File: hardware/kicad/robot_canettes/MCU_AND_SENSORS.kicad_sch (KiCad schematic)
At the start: 0 parts

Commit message: Ajout du STM32 et de son alimentation de base
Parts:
- added U1: STM32G431RBTx, Package_QFP:LQFP-64_10x10mm_P0.5mm, symbol MCU_ST_STM32G4:STM32G431RBTx
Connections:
- new net +3V3: U1.1 (VBAT), U1.16 (VDD), U1.28 (VREF+), U1.29 (VDDA), U1.32 (VDD), U1.48 (VDD), U1.64 (VDD)
- new net GND: U1.15 (VSS), U1.27 (VSSA), U1.31 (VSS), U1.47 (VSS), U1.63 (VSS)
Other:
- company: (none) -> ENSEA
- title: (none) -> MCU_AND_SENSORS

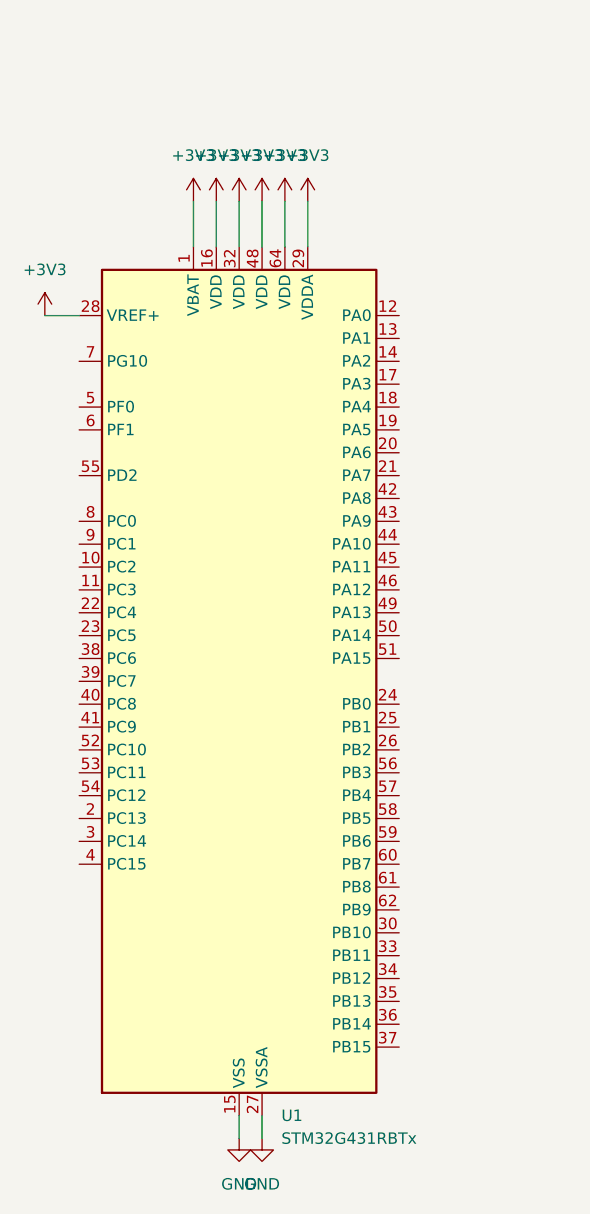
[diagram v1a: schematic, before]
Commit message: Ajout découplage VDD/VDDA/VBAT + condensateur NRST
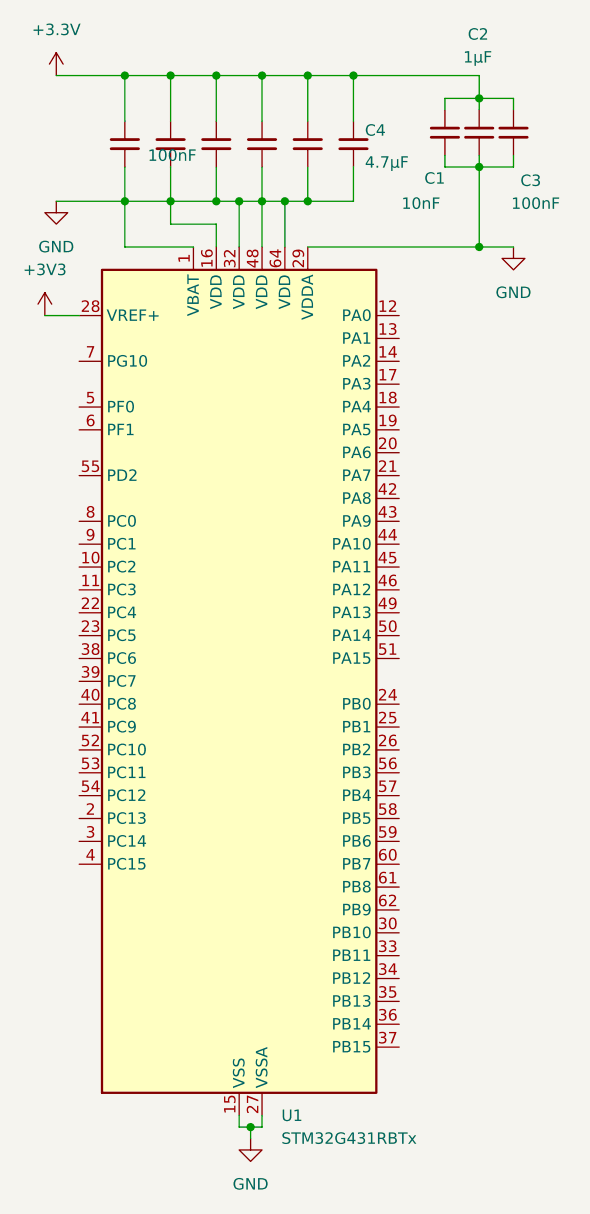
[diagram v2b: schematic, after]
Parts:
- added C1: 10nF, symbol Device:C_Small
- added C2: 1µF, symbol Device:C_Small
- added C3, C5, C6, C7, C8, C9: 100nF, symbol Device:C_Small
- added C4: 4.7µF, symbol Device:C_Small
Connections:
- net +3V3: no longer U1.1 (VBAT), U1.16 (VDD), U1.29 (VDDA), U1.32 (VDD), U1.48 (VDD), U1.64 (VDD)
- net GND: now also U1.1 (VBAT), U1.16 (VDD), U1.29 (VDDA), U1.32 (VDD), U1.48 (VDD), U1.64 (VDD), C1.2, C2.2, C3.2, C4.2, C5.2, C6.2, C7.2, C8.2, C9.2
- new net +3.3V: C1.1, C2.1, C3.1, C4.1, C5.1, C6.1, C7.1, C8.1, C9.1

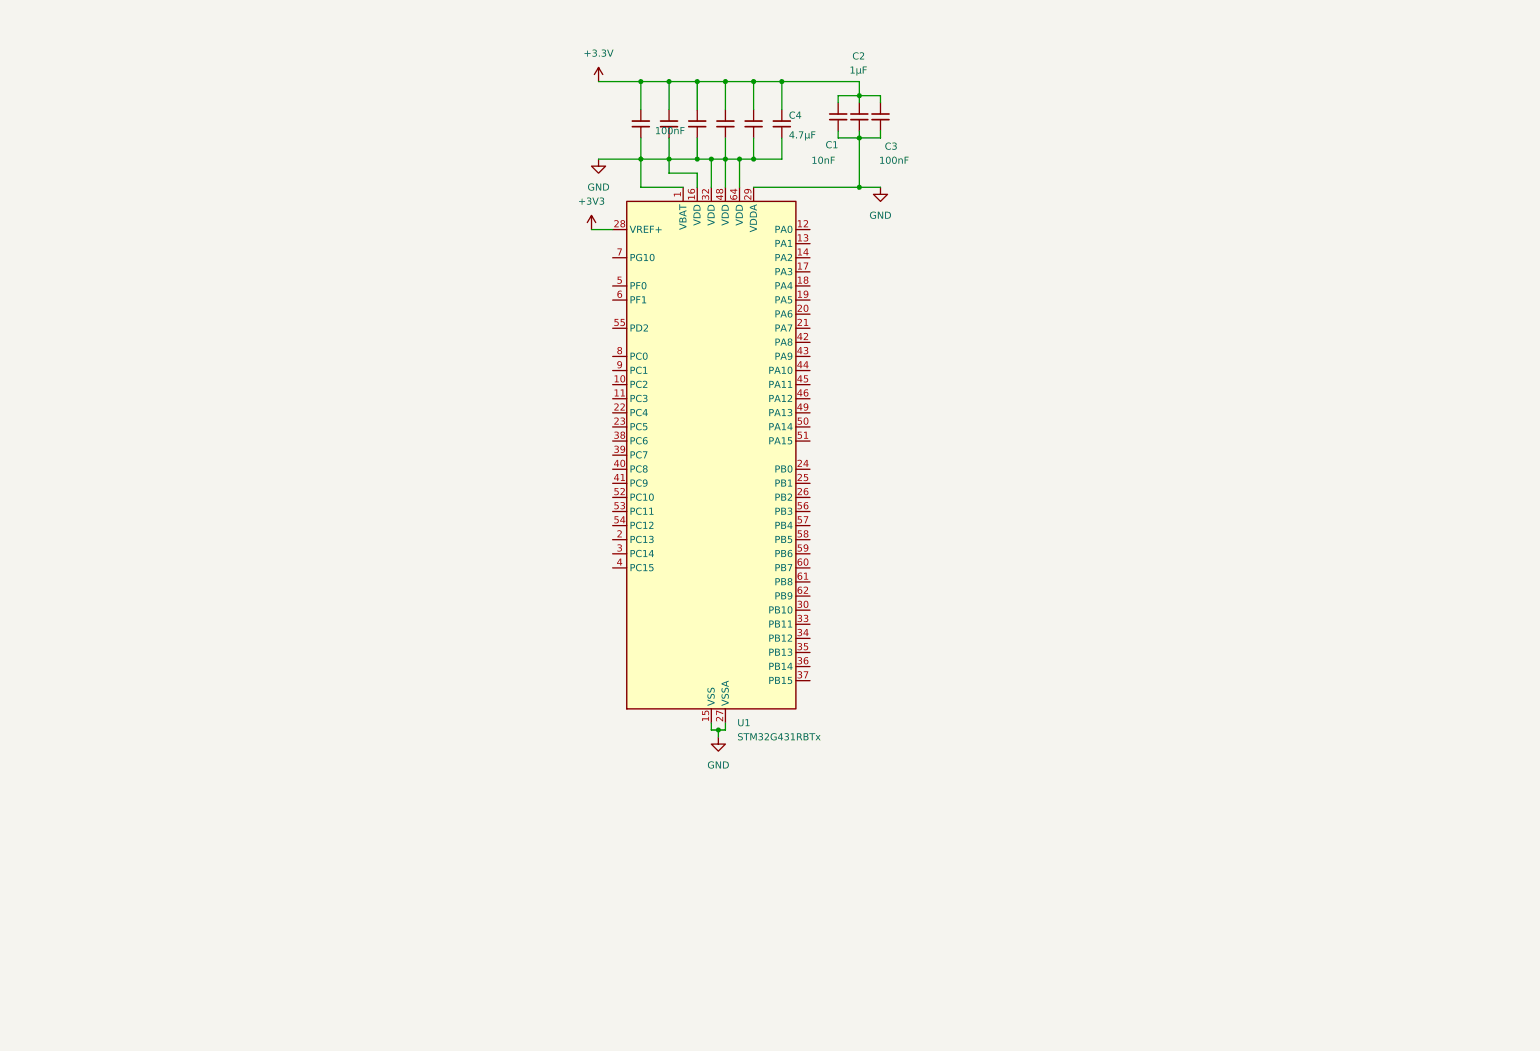
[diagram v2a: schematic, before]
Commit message: Ajout schema MCU et capteurs (02_MCU_AND_SENSORS)
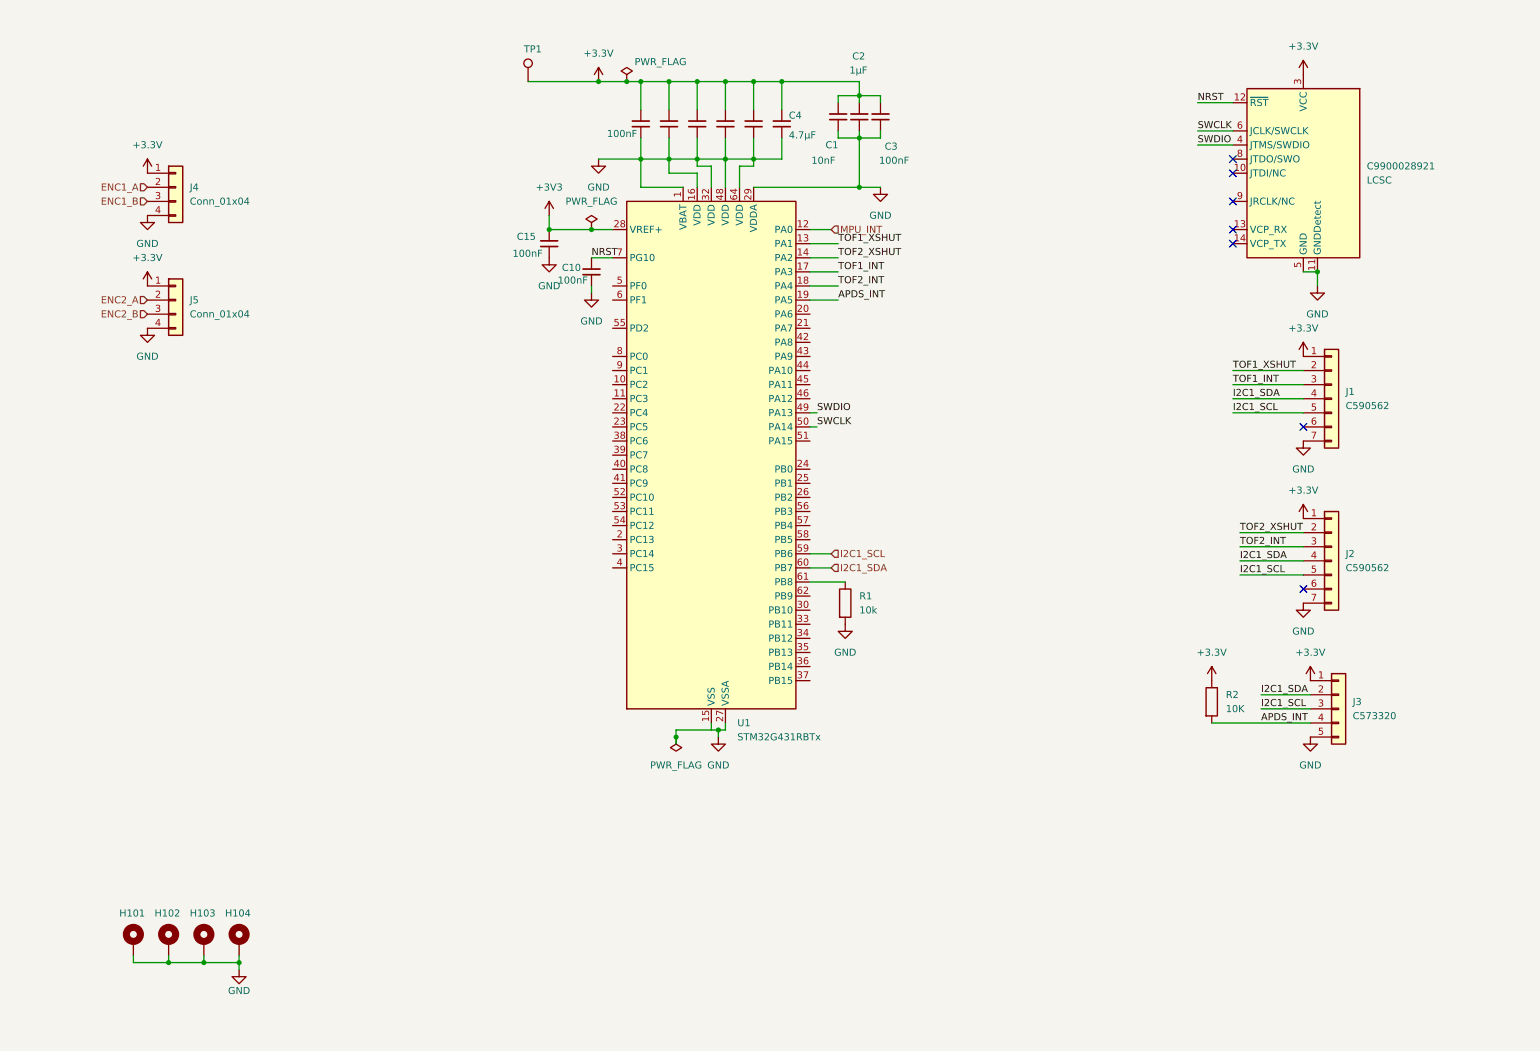
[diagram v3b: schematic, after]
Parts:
- added C10, C15: 100nF, symbol Device:C_Small
- added H101, H102, H103, H104: MountingHole_Pad, MountingHole:MountingHole_3.2mm_M3_Pad_Via, symbol Mechanical:MountingHole_Pad
- added J1, J2: C590562, symbol Connector_Generic:Conn_01x07
- added J3: C573320, symbol Connector_Generic:Conn_01x05
- added J4, J5: Conn_01x04, symbol Connector_Generic:Conn_01x04
- added LCSC: C9900028921, Package_TO_SOT_SMD:TO-252-2, symbol Connector:Conn_ST_STDC14
- added R1: 10k, symbol Device:R
- added R2: 10K, symbol Device:R
- added TP1: TestPoint, RF_Module:ESP32-S2-WROVER, symbol Connector:TestPoint
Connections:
- net +3.3V: now also J1.1 (VIN), J2.1 (Pin_1), J3.1 (Pin_1), J4.1 (Pin_1), J5.1 (Pin_1), LCSC.3 (VCC), R2.1, TP1.1
- net +3V3: now also C15.1
- net GND: now also C10.2, C15.2, H101.1, H102.1, H103.1, H104.1, J1.7 (Pin_7), J2.7 (Pin_7), J3.5 (Pin_5), J4.4 (Pin_4), J5.4 (Pin_4), LCSC.11 (GNDDetect), LCSC.5 (GND), LCSC.7 (GND), R1.2; no longer U1.15 (VSS), U1.31 (VSS), U1.47 (VSS), U1.63 (VSS)
- net MPU_INT: now reaches U1.12 (PA0)
- net TOF1_XSHUT: now reaches U1.13 (PA1)
- net TOF1_XSHUT: now also J1.2 (Pin_2)
- net TOF2_XSHUT: now reaches U1.14 (PA2)
- net TOF2_XSHUT: now also J2.2 (Pin_2)
- net TOF1_INT: now reaches U1.17 (PA3)
- net TOF1_INT: now also J1.3 (Pin_3)
- net TOF2_INT: now reaches U1.18 (PA4)
- net TOF2_INT: now also J2.3 (Pin_3)
- net APDS_INT: now reaches U1.19 (PA5)
- net APDS_INT: now also J3.4 (Pin_4), R2.2
- net SWDIO: now reaches U1.49 (PA13)
- net SWDIO: now also LCSC.4 (JTMS/SWDIO)
- net SWCLK: now reaches U1.50 (PA14)
- net SWCLK: now also LCSC.6 (JCLK/SWCLK)
- net I2C1_SCL: now reaches U1.59 (PB6)
- net I2C1_SCL: now also J1.5 (Pin_5), J2.5 (Pin_5), J3.3 (Pin_3)
- net I2C1_SDA: now reaches U1.60 (PB7)
- net I2C1_SDA: now also J1.4 (Pin_4), J2.4 (Pin_4), J3.2 (Pin_2)
- net at U1.61 (PB8): now also R1.1
- net NRST: now reaches U1.7 (PG10)
- net NRST: now also C10.1, LCSC.12 (~{RST})
- new net: U1.15 (VSS), U1.31 (VSS), U1.47 (VSS), U1.63 (VSS)
- new net ENC1_A: J4.2 (Pin_2)
- new net ENC1_B: J4.3 (Pin_3)
- new net ENC2_A: J5.2 (Pin_2)
- new net ENC2_B: J5.3 (Pin_3)
- no-connect marks 0 -> 7

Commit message: MAJ schema MCU/sensors
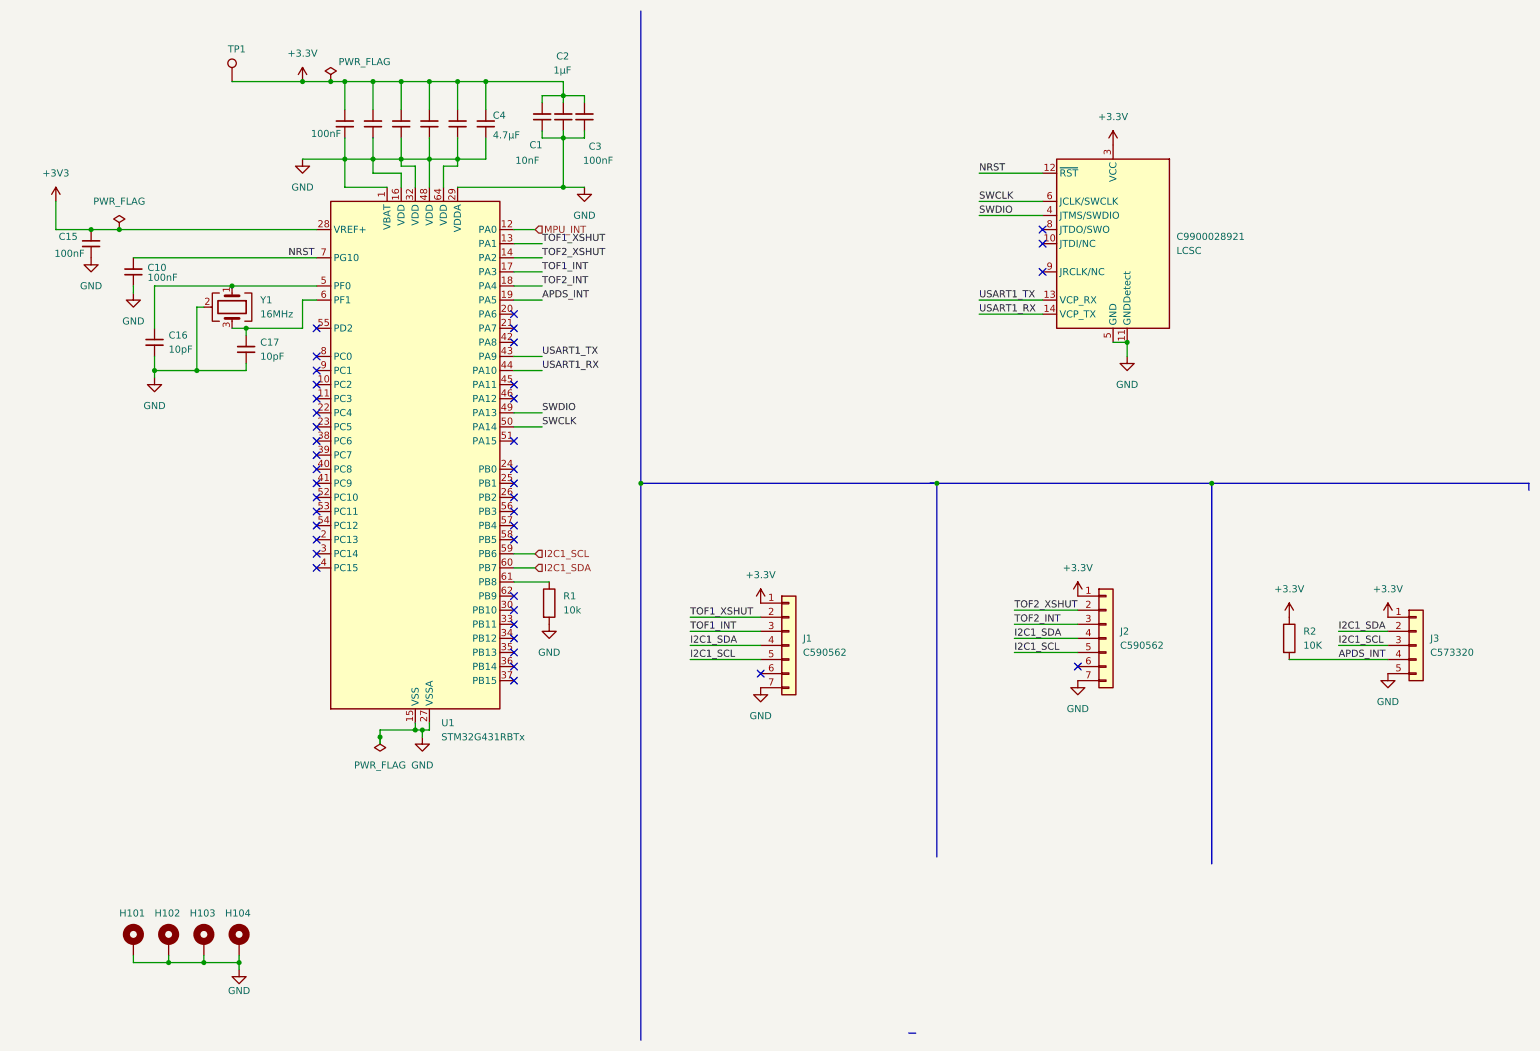
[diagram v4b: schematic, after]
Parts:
- removed J4, J5: Conn_01x04, symbol Connector_Generic:Conn_01x04
- added C16, C17: 10pF, Package_CSP:Xilinx_CSG48_7.0x7.0mm_Layout7x7_P0.8mm, symbol Device:C_Small
- added Y1: 16MHz, Crystal:Crystal_SMD_EuroQuartz_MT-4Pin_3.2x2.5mm, symbol Device:Crystal_GND24
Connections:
- net GND: now also U1.15 (VSS), U1.31 (VSS), U1.47 (VSS), U1.63 (VSS), C16.2, C17.2, Y1.2 (G), Y1.4 (G)
- net USART1_TX: now reaches LCSC.13 (VCP_RX)
- net USART1_TX: now also U1.43 (PA9)
- net USART1_RX: now reaches LCSC.14 (VCP_TX)
- net USART1_RX: now also U1.44 (PA10)
- net at U1.5 (PF0): now also C16.1, Y1.1
- net at U1.6 (PF1): now also C17.1, Y1.3
- no-connect marks 7 -> 41
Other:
- moved on the sheet: C1, C10, C15, C2, C3, C4, J1, J2, J3, LCSC, R1, R2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

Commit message: MAJ schema MCU/sensors
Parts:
- C1: JLCPCB PART# (none) -> C15195
- J1, J2: JLCPCB PART # (none) -> C590562
- J3: JLCPCB PART# (none) -> C573320
- LCSC: JLCPCB PART # (none) -> C9900028921
- U1: JLCPCB PART # (none) -> C431633
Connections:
- net MOTOR_SLEEP: now reaches U1.22 (PC4)
- net MOTOR_FAULT: now reaches U1.23 (PC5)
- net SERVO1_PWM: now reaches U1.36 (PB14)
- net MOTOR_B_C1: now reaches U1.38 (PC6)
- net MOTOR_B_C2: now reaches U1.39 (PC7)
- net I2C3_SCL: now reaches U1.40 (PC8)
- net I2C3_SCL: now also J1.5 (Pin_5), J2.5 (Pin_5), J3.3 (Pin_3)
- net I2C3_SDA: now reaches U1.41 (PC9)
- net I2C3_SDA: now also J1.4 (Pin_4), J2.4 (Pin_4), J3.2 (Pin_2)
- net MOTOR_B_IN1: now reaches U1.42 (PA8)
- net MOTOR_B_IN2: now reaches U1.45 (PA11)
- net MOTOR_A_C1: now reaches U1.51 (PA15)
- net MOTOR_A_C2: now reaches U1.56 (PB3)
- net MOTOR_A_IN1: now reaches U1.57 (PB4)
- net MOTOR_A_IN2: now reaches U1.58 (PB5)
- removed net I2C1_SCL: J1.5 (Pin_5), J2.5 (Pin_5), J3.3 (Pin_3), U1.59 (PB6)
- removed net I2C1_SDA: J1.4 (Pin_4), J2.4 (Pin_4), J3.2 (Pin_2), U1.60 (PB7)
- no-connect marks 41 -> 30
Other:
- note added: "CONN_MPU"
- note added: "CONN_TOF1"
- note added: "CONN_TOF2"
- note added: "STM32G431RBTx"
- note added: "SWD"
- moved on the sheet: C1, C10, C15, C16, C17, C2, C3, C4, R1, TP1, U1, Y1
